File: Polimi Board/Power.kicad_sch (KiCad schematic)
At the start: 7 parts, among them J4 Jack-DC, U5 MCP1826S, U6 MCP1826S

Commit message: Update the design with new specifications
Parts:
- removed C24, C25, C26, C27: C, symbol Device:C
- removed J4: Jack-DC, Connector_BarrelJack:BarrelJack_SwitchcraftConxall_RAPC10U_Horizontal, symbol Connector:Jack-DC
- removed U5, U6: MCP1826S, Package_TO_SOT_SMD:SOT-223-3_TabPin2, symbol Regulator_Linear:MCP1826S
- added C29, C30, C31, C32: C, symbol Device:C
- added D6: ~, symbol Device:D
- added J8: Jack-DC, Connector_BarrelJack:BarrelJack_SwitchcraftConxall_RAPC10U_Horizontal, symbol Connector:Jack-DC
- added Q1: FDN340P, Package_TO_SOT_SMD:SOT-23, symbol Transistor_FET:FDN340P
- added R36, R37: 10k, symbol Device:R
- added SW9: SW_DIP_x01, symbol Switch:SW_DIP_x01
- added U4, U7: MCP1826S, Package_TO_SOT_SMD:SOT-223-3_TabPin2, symbol Regulator_Linear:MCP1826S
- added U5, U6, U8: LM358, symbol Amplifier_Operational:LM358
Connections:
- net +3.3V: now also C31.1, U4.3 (VO), U5.2 (-)
- net GND: now also C29.2, C30.2, C31.2, C32.2, J8.2, R37.2, U4.2 (GND), U7.2 (GND), U8.4 (V-)
- new net: D6.2 (A), SW9.2
- new net: J8.1, SW9.1
- new net: Q1.1 (G), U5.1
- new net: R36.2, R37.1, U5.3 (+)
- new net +5V: C29.1, C32.1, Q1.2 (S), U4.1 (VI), U7.3 (VO), U8.8 (V+)
- new net USB_Vcc: Q1.3 (D)
- new net Vin: C30.1, D6.1 (K), R36.1, U7.1 (VI)
- no-connect marks 0 -> 3
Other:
- note added: "Comparator"
- note added: "This is the same circuit of ARDUINO UNO Rev.3 for using USB if it is the only one power source or Barrel Jack if available"
- note added: "Total power consumption estimation = ~300mA"

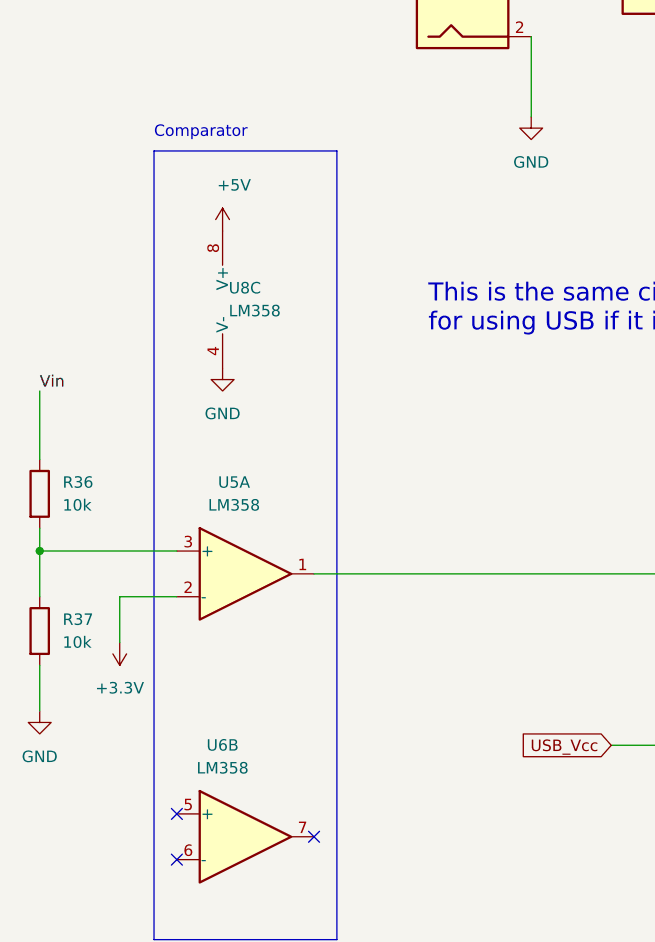
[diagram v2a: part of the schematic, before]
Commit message: Update resets and readme
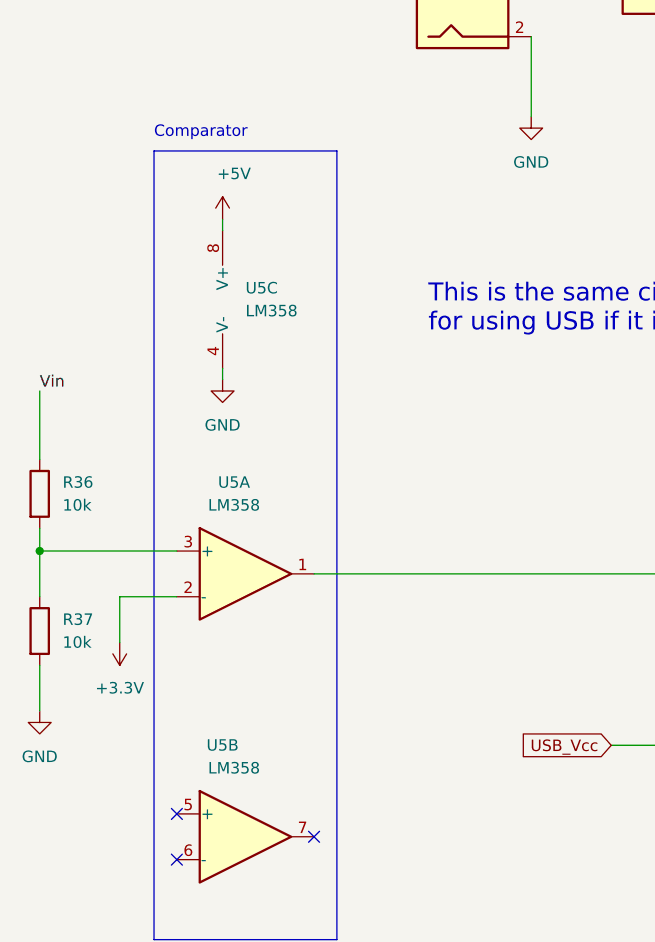
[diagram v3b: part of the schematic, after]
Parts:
- renumbered U8 to U5, U6 to U5
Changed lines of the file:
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@@
   (title_block
     (title "Polimi Board ")
-    (date "2024-05-14")
+    (date "2024-05-15")
     (rev "2.0")
     (company "Politecnico di Milano")
@@
     (stroke (width 0) (type default))
   )
+  (wire (pts (xy 77.47 76.2) (xy 77.47 77.47))
+    (stroke (width 0) (type default))
+  )
   (wire (pts (xy 191.77 143.51) (xy 191.77 148.59))
     (stroke (width 0) (type default))
@@
   )
   (wire (pts (xy 120.65 134.62) (xy 127 134.62))
+    (stroke (width 0) (type default))
+  )
+  (wire (pts (xy 77.47 93.98) (xy 77.47 92.71))
     (stroke (width 0) (type default))
   )
@@
     )
   )
-  (symbol (lib_id "power:+5V") (at 77.47 77.47 0) (unit 1)
+  (symbol (lib_id "power:+5V") (at 77.47 76.2 0) (unit 1)
     (in_bom yes) (on_board yes) (dnp no)
-    (property "Reference" "#PWR065" (at 77.47 81.28 0)
-      (effects (font (size 1.27 1.27)) hide)
-    )
-    (property "Value" "+5V" (at 78.74 72.39 0)
-      (effects (font (size 1.27 1.27)))
-    )
-    (property "Footprint" "" (at 77.47 77.47 0)
-      (effects (font (size 1.27 1.27)) hide)
-    )
-    (property "Datasheet" "" (at 77.47 77.47 0)
+    (property "Reference" "#PWR065" (at 77.47 80.01 0)
+      (effects (font (size 1.27 1.27)) hide)
+    )
+    (property "Value" "+5V" (at 78.74 71.12 0)
+      (effects (font (size 1.27 1.27)))
+    )
+    (property "Footprint" "" (at 77.47 76.2 0)
+      (effects (font (size 1.27 1.27)) hide)
+    )
+    (property "Datasheet" "" (at 77.47 76.2 0)
       (effects (font (size 1.27 1.27)) hide)
     )
@@
   )
   (symbol (lib_id "Amplifier_Operational:LM358") (at 80.01 85.09 0) (unit 3)
-    (in_bom yes) (on_board yes) (dnp no) (fields_autoplaced)
-    (property "Reference" "U8" (at 78.1401 83.82 0)
-      (effects (font (size 1.27 1.27)) (justify left))
-    )
-    (property "Value" "LM358" (at 78.1401 86.36 0)
+    (in_bom yes) (on_board yes) (dnp no)
+    (property "Reference" "U5" (at 80.01 83.82 0)
+      (effects (font (size 1.27 1.27)) (justify left))
+    )
+    (property "Value" "LM358" (at 80.01 86.36 0)
       (effects (font (size 1.27 1.27)) (justify left))
     )
@@
       (project "Polimi Board"
         (path "/319fe76e-1f98-44b3-99b0-af1a9ad7322c/2829f40f-8e49-4037-a7dc-c950fd3c5b99"
-          (reference "U8") (unit 3)
+          (reference "U5") (unit 3)
         )
       )
@@
   (symbol (lib_id "Amplifier_Operational:LM358") (at 80.01 144.78 0) (unit 2)
     (in_bom yes) (on_board yes) (dnp no)
-    (property "Reference" "U6" (at 77.47 134.62 0)
-      (effects (font (size 1.27 1.27)))
-    )
-    (property "Value" "LM358" (at 77.47 137.16 0)
+    (property "Reference" "U5" (at 77.47 134.62 0)
+      (effects (font (size 1.27 1.27)))
+    )
+    (property "Value" "LM358" (at 78.74 137.16 0)
       (effects (font (size 1.27 1.27)))
     )
@@
       (project "Polimi Board"
         (path "/319fe76e-1f98-44b3-99b0-af1a9ad7322c/2829f40f-8e49-4037-a7dc-c950fd3c5b99"
-          (reference "U6") (unit 2)
+          (reference "U5") (unit 2)
         )
       )
@@
     )
   )
-  (symbol (lib_id "power:GND") (at 77.47 92.71 0) (unit 1)
-    (in_bom yes) (on_board yes) (dnp no) (fields_autoplaced)
-    (property "Reference" "#PWR052" (at 77.47 99.06 0)
-      (effects (font (size 1.27 1.27)) hide)
-    )
-    (property "Value" "GND" (at 77.47 97.79 0)
-      (effects (font (size 1.27 1.27)))
-    )
-    (property "Footprint" "" (at 77.47 92.71 0)
-      (effects (font (size 1.27 1.27)) hide)
-    )
-    (property "Datasheet" "" (at 77.47 92.71 0)
-      (effects (font (size 1.27 1.27)) hide)
-    )
+  (symbol (lib_id "power:GND") (at 77.47 93.98 0) (unit 1)
+    (in_bom yes) (on_board yes) (dnp no) (fields_autoplaced)
+    (property "Reference" "#PWR052" (at 77.47 100.33 0)
+      (effects (font (size 1.27 1.27)) hide)
+    )
+    (property "Value" "GND" (at 77.47 99.06 0)
+      (effects (font (size 1.27 1.27)))
+    )
+    (property "Footprint" "" (at 77.47 93.98 0)
+      (effects (font (size 1.27 1.27)) hide)
+    )
+    (property "Datasheet" "" (at 77.47 93.98 0)
+      (effects (font (size 1.27 1.27)) hide)
+    )

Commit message: Added changes to the design
Ready for pcb design
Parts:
- removed C30, C32: C, symbol Device:C
- removed D6: ~, symbol Device:D
- removed J8: Jack-DC, Connector_BarrelJack:BarrelJack_SwitchcraftConxall_RAPC10U_Horizontal, symbol Connector:Jack-DC
- removed Q1: FDN340P, Package_TO_SOT_SMD:SOT-23, symbol Transistor_FET:FDN340P
- removed R36, R37: 10k, symbol Device:R
- removed SW9: SW_DIP_x01, symbol Switch:SW_DIP_x01
- removed U5: LM358, symbol Amplifier_Operational:LM358
- removed U7: MCP1826S, Package_TO_SOT_SMD:SOT-223-3_TabPin2, symbol Regulator_Linear:MCP1826S
- C29: value C -> 47uF
- C31: value C -> 10uF
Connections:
- no-connect marks 3 -> 0
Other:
- note added: "Power from USB at 5V already filtered"
- note removed: "Comparator"
- note removed: "This is the same circuit of ARDUINO UNO Rev.3 for using USB if it is the only one power source or Barrel Jack if available"
- moved on the sheet: C29, C31, U4

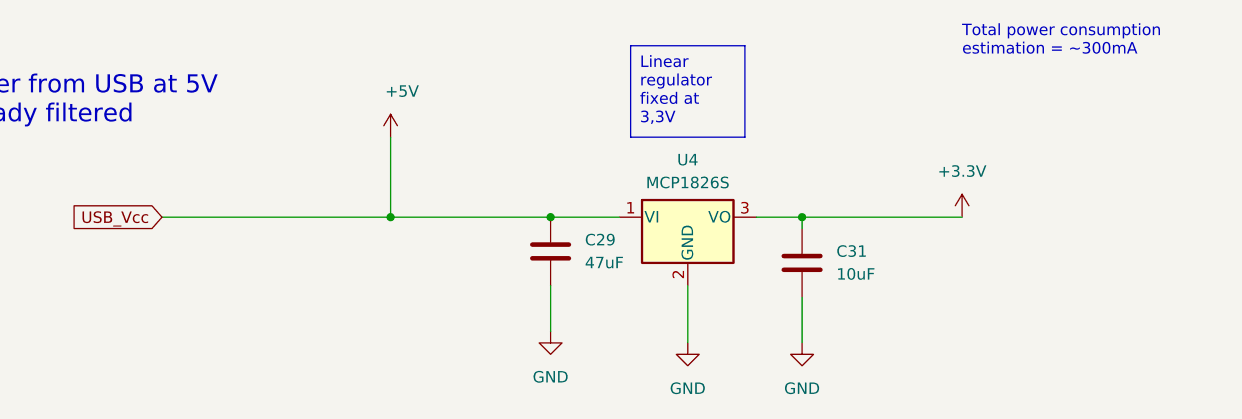
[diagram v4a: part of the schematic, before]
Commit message: adjusted some violations of ERC test
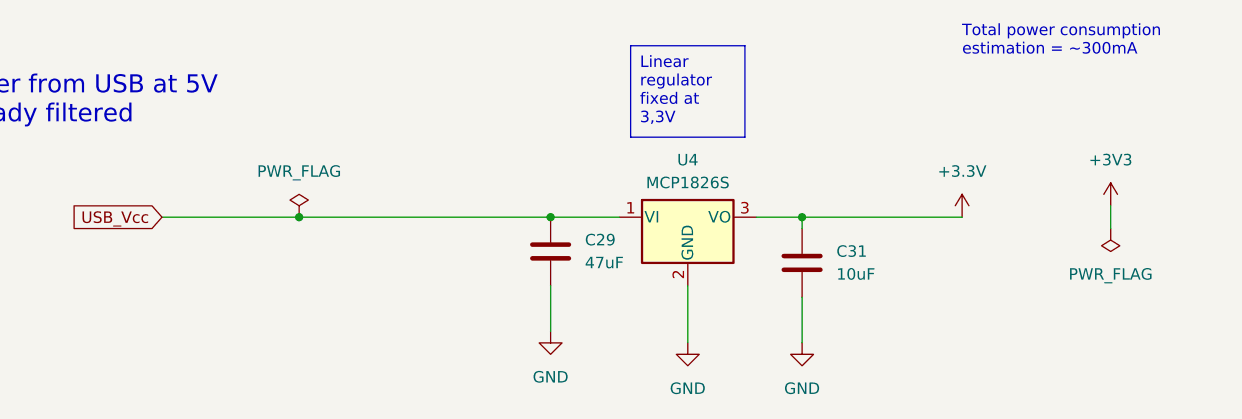
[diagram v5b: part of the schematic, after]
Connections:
- net +5V renamed USB_Vcc
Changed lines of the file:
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@@
     (comment 2 "ing. Zaccaria Eliseo Carrettoni")
   )
-  (junction (at 132.08 97.79) (diameter 0) (color 0 0 0 0)
+  (junction (at 121.92 97.79) (diameter 0) (color 0 0 0 0)
   )
   (junction (at 149.86 97.79) (diameter 0) (color 0 0 0 0)
@@
   (junction (at 177.8 97.79) (diameter 0) (color 0 0 0 0)
   )
-  (wire (pts (xy 132.08 88.9) (xy 132.08 97.79))
-    (stroke (width 0) (type default))
-  )
   (wire (pts (xy 172.72 97.79) (xy 177.8 97.79))
     (stroke (width 0) (type default))
@@
     (stroke (width 0) (type default))
   )
-  (wire (pts (xy 132.08 97.79) (xy 149.86 97.79))
+  (wire (pts (xy 121.92 97.79) (xy 149.86 97.79))
     (stroke (width 0) (type default))
   )
@@
     (stroke (width 0) (type default))
   )
-  (wire (pts (xy 106.68 97.79) (xy 132.08 97.79))
+  (wire (pts (xy 212.09 96.52) (xy 212.09 99.06))
     (stroke (width 0) (type default))
   )
@@
   )
   (wire (pts (xy 149.86 97.79) (xy 157.48 97.79))
+    (stroke (width 0) (type default))
+  )
+  (wire (pts (xy 106.68 97.79) (xy 121.92 97.79))
     (stroke (width 0) (type default))
   )
@@
     )
   )
+  (symbol (lib_id "power:+3V3") (at 212.09 96.52 0) (unit 1)
+    (in_bom yes) (on_board yes) (dnp no) (fields_autoplaced)
+    (property "Reference" "#PWR021" (at 212.09 100.33 0)
+      (effects (font (size 1.27 1.27)) hide)
+    )
+    (property "Value" "+3V3" (at 212.09 91.44 0)
+      (effects (font (size 1.27 1.27)))
+    )
+    (property "Footprint" "" (at 212.09 96.52 0)
+      (effects (font (size 1.27 1.27)) hide)
+    )
+    (property "Datasheet" "" (at 212.09 96.52 0)
+      (effects (font (size 1.27 1.27)) hide)
+    )
+    (pin "1")
+    (instances
+      (project "Polimi Board"
+        (path "/319fe76e-1f98-44b3-99b0-af1a9ad7322c/2829f40f-8e49-4037-a7dc-c950fd3c5b99"
+          (reference "#PWR021") (unit 1)
+        )
+      )
+    )
+  )
+  (symbol (lib_id "power:PWR_FLAG") (at 121.92 97.79 0) (unit 1)
+    (in_bom yes) (on_board yes) (dnp no) (fields_autoplaced)
+    (property "Reference" "#FLG04" (at 121.92 95.885 0)
+      (effects (font (size 1.27 1.27)) hide)
+    )
+    (property "Value" "PWR_FLAG" (at 121.92 92.71 0)
+      (effects (font (size 1.27 1.27)))
+    )
+    (property "Footprint" "" (at 121.92 97.79 0)
+      (effects (font (size 1.27 1.27)) hide)
+    )
+    (property "Datasheet" "~" (at 121.92 97.79 0)
+      (effects (font (size 1.27 1.27)) hide)
+    )
+    (pin "1")
+    (instances
+      (project "Polimi Board"
+        (path "/319fe76e-1f98-44b3-99b0-af1a9ad7322c/2829f40f-8e49-4037-a7dc-c950fd3c5b99"
+          (reference "#FLG04") (unit 1)
+        )
+      )
+    )
+  )
   (symbol (lib_id "power:GND") (at 165.1 111.76 0) (unit 1)
     (in_bom yes) (on_board yes) (dnp no) (fields_autoplaced)
@@
     )
   )
+  (symbol (lib_id "power:PWR_FLAG") (at 212.09 99.06 180) (unit 1)
+    (in_bom yes) (on_board yes) (dnp no) (fields_autoplaced)
+    (property "Reference" "#FLG02" (at 212.09 100.965 0)
+      (effects (font (size 1.27 1.27)) hide)
+    )
+    (property "Value" "PWR_FLAG" (at 212.09 104.14 0)
+      (effects (font (size 1.27 1.27)))
+    )
+    (property "Footprint" "" (at 212.09 99.06 0)
+      (effects (font (size 1.27 1.27)) hide)
+    )
+    (property "Datasheet" "~" (at 212.09 99.06 0)
+      (effects (font (size 1.27 1.27)) hide)
+    )
+    (pin "1")
+    (instances
+      (project "Polimi Board"
+        (path "/319fe76e-1f98-44b3-99b0-af1a9ad7322c/2829f40f-8e49-4037-a7dc-c950fd3c5b99"
+          (reference "#FLG02") (unit 1)
+        )
+      )
+    )
+  )
   (symbol (lib_id "power:GND") (at 149.86 110.49 0) (unit 1)
     (in_bom yes) (on_board yes) (dnp no) (fields_autoplaced)
@@
         )
       )
-    )
-  )
-  (symbol (lib_id "power:+5V") (at 132.08 88.9 0) (unit 1)
-    (in_bom yes) (on_board yes) (dnp no)
-    (property "Reference" "#PWR062" (at 132.08 92.71 0)
-      (effects (font (size 1.27 1.27)) hide)
-    )
-    (property "Value" "+5V" (at 133.35 83.82 0)
-      (effects (font (size 1.27 1.27)))
-    )
-    (property "Footprint" "" (at 132.08 88.9 0)
-      (effects (font (size 1.27 1.27)) hide)
-    )
-    (property "Datasheet" "" (at 132.08 88.9 0)
-      (effects (font (size 1.27 1.27)) hide)
-    )
-    (pin "1")
-    (instances
-      (project "Polimi Board"
-        (path "/319fe76e-1f98-44b3-99b0-af1a9ad7322c/2829f40f-8e49-4037-a7dc-c950fd3c5b99"
-          (reference "#PWR062") (unit 1)
-        )
-      )

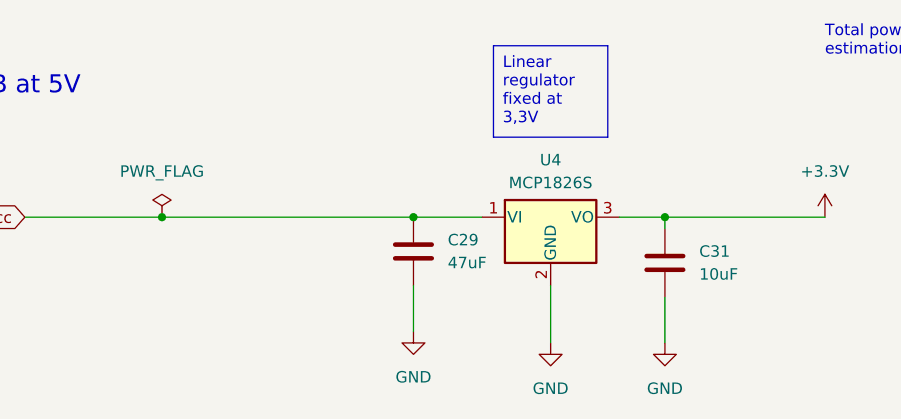
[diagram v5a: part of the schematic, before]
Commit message: Added footprint from Mouser
readu for wiring
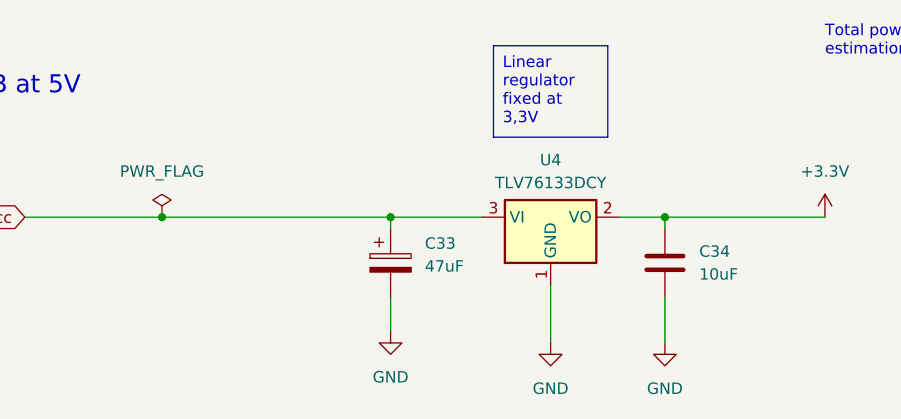
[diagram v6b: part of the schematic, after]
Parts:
- removed C29: 47uF, symbol Device:C
- removed U4: MCP1826S, Package_TO_SOT_SMD:SOT-223-3_TabPin2, symbol Regulator_Linear:MCP1826S
- added C33: 47uF, Capacitor_THT:CP_Radial_D8.0mm_P3.50mm, symbol Device:C_Polarized
- added U4: TLV76133DCY, Package_TO_SOT_SMD:SOT-223-3_TabPin2, symbol Regulator_Linear:TLV76133DCY
- C34: renamed from C31; footprint (none) -> Capacitor_SMD:C_0603_1608Metric_Pad1.08x0.95mm_HandSolder
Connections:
- net +3.3V: now also U4.2 (VO)
- net GND: now also C33.2, U4.1 (GND)
- net USB_Vcc: now also C33.1, U4.3 (VI)

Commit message: PCB wip
before holidays
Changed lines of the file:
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@@
-	(wire
-		(pts
-			(xy 212.09 96.52) (xy 212.09 99.06)
-		)
-		(stroke
-			(width 0)
-			(type default)
-		)
-	)
 	(wire
 		(pts
@@
 	)
 	(symbol
-		(lib_id "power:+3V3")
-		(at 212.09 96.52 0)
-		(unit 1)
-		(exclude_from_sim no)
-		(in_bom yes)
-		(on_board yes)
-		(dnp no)
-		(fields_autoplaced yes)
-		(property "Reference" "#PWR090"
-			(at 212.09 100.33 0)
-			(effects
-				(font
-					(size 1.27 1.27)
-				)
-				(hide yes)
-			)
-		)
-		(property "Value" "+3V3"
-			(at 212.09 91.44 0)
-			(effects
-				(font
-					(size 1.27 1.27)
-				)
-			)
-		)
-		(property "Footprint" ""
-			(at 212.09 96.52 0)
-			(effects
-				(font
-					(size 1.27 1.27)
-				)
-				(hide yes)
-			)
-		)
-		(property "Datasheet" ""
-			(at 212.09 96.52 0)
-			(effects
-				(font
-					(size 1.27 1.27)
-				)
-				(hide yes)
-			)
-		)
-		(property "Description" ""
-			(at 212.09 96.52 0)
-			(effects
-				(font
-					(size 1.27 1.27)
-				)
-				(hide yes)
-			)
-		)
-		(pin "1"
-		)
-		(instances
-			(project "Polimi Board"
-				(path "/319fe76e-1f98-44b3-99b0-af1a9ad7322c/2829f40f-8e49-4037-a7dc-c950fd3c5b99"
-					(reference "#PWR090")
-					(unit 1)
-				)
-			)
-		)
-	)
-	(symbol
 		(lib_id "Regulator_Linear:TLV76133DCY")
 		(at 165.1 97.79 0)
@@
 					(unit 1)
 				)
-			)
-		)
-	)
-	(symbol
-		(lib_id "power:PWR_FLAG")
-		(at 212.09 99.06 180)
-		(unit 1)
-		(exclude_from_sim no)
-		(in_bom yes)
-		(on_board yes)
-		(dnp no)
-		(fields_autoplaced yes)
-		(property "Reference" "#FLG03"
-			(at 212.09 100.965 0)
-			(effects
-				(font
-					(size 1.27 1.27)
-				)
-				(hide yes)
-			)
-		)
-		(property "Value" "PWR_FLAG"
-			(at 212.09 104.14 0)
-			(effects
-				(font
-					(size 1.27 1.27)
-				)
-			)
-		)
-		(property "Footprint" ""
-			(at 212.09 99.06 0)
-			(effects
-				(font
-					(size 1.27 1.27)
-				)
-				(hide yes)
-			)
-		)
-		(property "Datasheet" "~"
-			(at 212.09 99.06 0)
-			(effects
-				(font
-					(size 1.27 1.27)
-				)
-				(hide yes)
-			)
-		)
-		(property "Description" ""
-			(at 212.09 99.06 0)
-			(effects
-				(font
-					(size 1.27 1.27)
-				)
-				(hide yes)
-			)
-		)
-		(pin "1"
-		)
-		(instances
-			(project "Polimi Board"
-				(path "/319fe76e-1f98-44b3-99b0-af1a9ad7322c/2829f40f-8e49-4037-a7dc-c950fd3c5b99"
-					(reference "#FLG03")
-					(unit 1)
-				)
